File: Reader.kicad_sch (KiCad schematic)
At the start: 42 parts, among them J1 Conn_01x04, J2 Amphenol Dubox ‎76383-402LF‎, J3 Conn_01x04, J4 Conn_01x08, J5 Conn_01x10, J6 Conn_01x03, J7 Conn_01x02, Q1 2N7002, Q2 2N7002, Q3 2N7002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

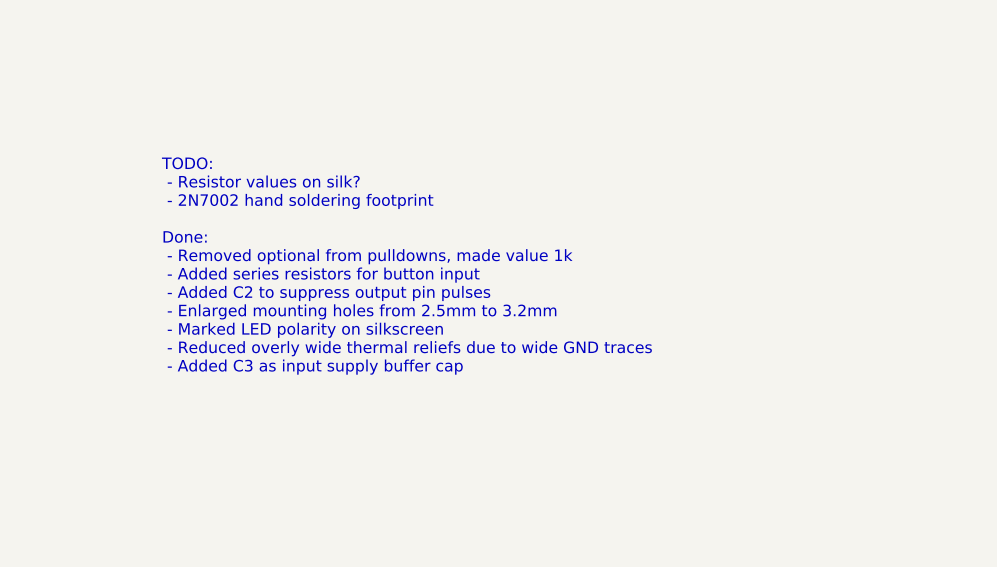
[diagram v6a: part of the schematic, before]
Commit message: Use hand soldering footprints for transistors
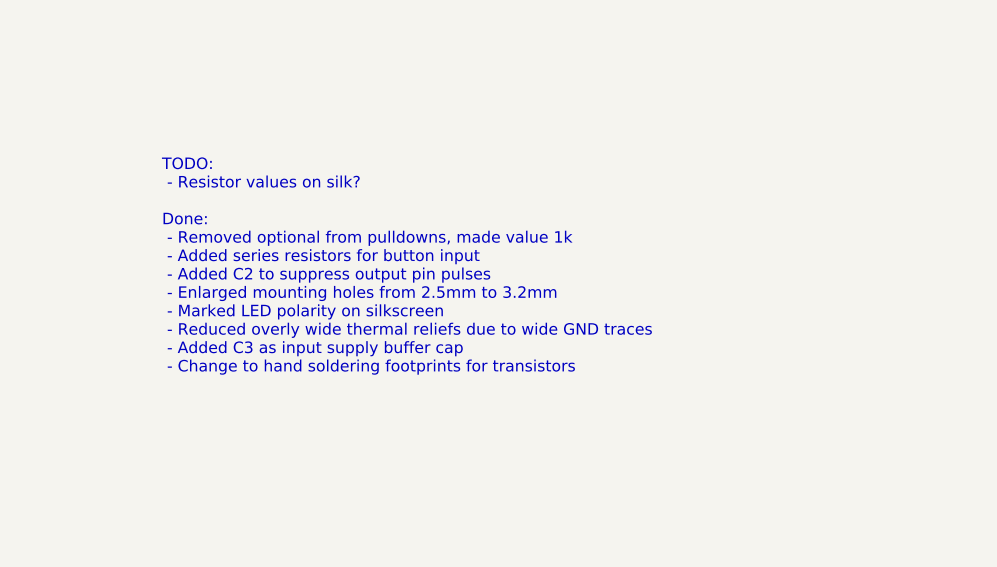
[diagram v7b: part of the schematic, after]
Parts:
- Q1, Q2, Q3, Q4, Q5, Q6: footprint Package_TO_SOT_SMD:SOT-23 -> Package_TO_SOT_SMD:SOT-23_Handsoldering
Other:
- note added: "TODO: - Resistor values on silk? Done: - Removed optional from pulldowns, made value 1k - Added series resistors for button input - Added C2 to suppress output pin pulses - Enlarged mounting holes from 2.5mm to 3.2mm - Marked LED polarity on silkscreen - Reduced overly wide thermal reliefs due to wide GND traces - Added C3 as input supply buffer cap - Change to hand soldering footprints for trans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"
- note removed: "TODO: - Resistor values on silk? - 2N7002 hand soldering footprint Done: - Removed optional from pulldowns, made value 1k - Added series resistors for button input - Added C2 to suppress output pin pulses - Enlarged mounting holes from 2.5mm to 3.2mm - Marked LED polarity on silkscreen - Reduced overly wide thermal reliefs due to wide GND traces - Added C3 as input supply buffer cap"
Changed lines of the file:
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@@
     (stroke (width 0) (type default))
   )
-  (text "TODO:\n - Resistor values on silk?\n - 2N7002 hand soldering footprint\n\nDone:\n - Removed optional from pulldowns, made value 1k\n - Added series resistors for button input\n - Added C2 to suppress output pin pulses\n - Enlarged mounting holes from 2.5mm to 3.2mm\n - Marked LED polarity on silkscreen\n - Reduced overly wide thermal reliefs due to wide GND traces\n - Added C3 as input supply buffer cap"
+  (text "TODO:\n - Resistor values on silk?\n\nDone:\n - Removed optional from pulldowns, made value 1k\n - Added series resistors for button input\n - Added C2 to suppress output pin pulses\n - Enlarged mounting holes from 2.5mm to 3.2mm\n - Marked LED polarity on silkscreen\n - Reduced overly wide thermal reliefs due to wide GND traces\n - Added C3 as input supply buffer cap\n - Change to hand soldering footprints for transistors"
     (at 116.84 152.4 0)
     (effects (font (size 1.27 1.27)) (justify left bottom))
@@
       (effects (font (size 1.27 1.27)) (justify left))
     )
-    (property "Footprint" "Package_TO_SOT_SMD:SOT-23" (at 154.94 48.895 0)
+    (property "Footprint" "Package_TO_SOT_SMD:SOT-23_Handsoldering" (at 154.94 48.895 0)
       (effects (font (size 1.27 1.27) italic) (justify left) hide)
     )
@@
       (effects (font (size 1.27 1.27)) (justify left))
     )
-    (property "Footprint" "Package_TO_SOT_SMD:SOT-23" (at 59.69 128.905 0)
+    (property "Footprint" "Package_TO_SOT_SMD:SOT-23_Handsoldering" (at 59.69 128.905 0)
       (effects (font (size 1.27 1.27) italic) (justify left) hide)
     )
@@
       (effects (font (size 1.27 1.27)) (justify left))
     )
-    (property "Footprint" "Package_TO_SOT_SMD:SOT-23" (at 220.98 48.895 0)
+    (property "Footprint" "Package_TO_SOT_SMD:SOT-23_Handsoldering" (at 220.98 48.895 0)
       (effects (font (size 1.27 1.27) italic) (justify left) hide)
     )
@@
       (effects (font (size 1.27 1.27)) (justify left))
     )
-    (property "Footprint" "Package_TO_SOT_SMD:SOT-23" (at 154.94 97.155 0)
+    (property "Footprint" "Package_TO_SOT_SMD:SOT-23_Handsoldering" (at 154.94 97.155 0)
       (effects (font (size 1.27 1.27) italic) (justify left) hide)
     )
@@
       (effects (font (size 1.27 1.27)) (justify left))
     )
-    (property "Footprint" "Package_TO_SOT_SMD:SOT-23" (at 203.2 48.895 0)
+    (property "Footprint" "Package_TO_SOT_SMD:SOT-23_Handsoldering" (at 203.2 48.895 0)
       (effects (font (size 1.27 1.27) italic) (justify left) hide)
     )
@@
       (effects (font (size 1.27 1.27)) (justify left))
     )
-    (property "Footprint" "Package_TO_SOT_SMD:SOT-23" (at 203.2 97.155 0)
+    (property "Footprint" "Package_TO_SOT_SMD:SOT-23_Handsoldering" (at 203.2 97.155 0)
       (effects (font (size 1.27 1.27) italic) (justify left) hide)
     )
